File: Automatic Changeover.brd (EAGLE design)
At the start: 160 x 148.3 mm, 49 parts, among them IC1 ACS750LCA-050, IC2 XMEGA16A4A, IC4 ACS750LCA-050, IC5 ACS750LCA-050, K1 S216SE1, K2 S216SE1, K3 S216SE1, K4 S216SE1, K5 S216SE1, K6 S216SE1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

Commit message: good arrangement
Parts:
- moved IC1 74.3 mm to (142.2, 66.0), turned to 180 degrees
- moved T4 57.5 mm to (88.9, 111.8), turned to 90 degrees
- moved K1 49.5 mm to (132.1, 125.7), turned to 0 degrees
- moved B1 48.4 mm to (135.9, 10.2), turned to 180 degrees
- moved K3 46.0 mm to (87.6, 125.7), turned to 0 degrees
- moved T3 40.3 mm to (111.8, 111.8), turned to 90 degrees
- moved IC4 36.6 mm to (114.3, 66.0), turned to 180 degrees
- moved K2 36.1 mm to (110.5, 125.7), turned to 0 degrees
- moved T1 35.2 mm to (132.1, 110.5), turned to 90 degrees
- moved K4 34.3 mm to (88.9, 99.1), turned to 180 degrees
- moved C4 33.2 mm to (135.9, 50.8), turned to 180 degrees
- moved K6 29.2 mm to (133.3, 99.1), turned to 180 degrees
- moved B3 18.2 mm to (135.9, 25.4), turned to 180 degrees
- moved IC5 16.5 mm to (86.4, 66.0), turned to 180 degrees
- moved B4 13.3 mm to (135.9, 40.6), turned to 180 degrees
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
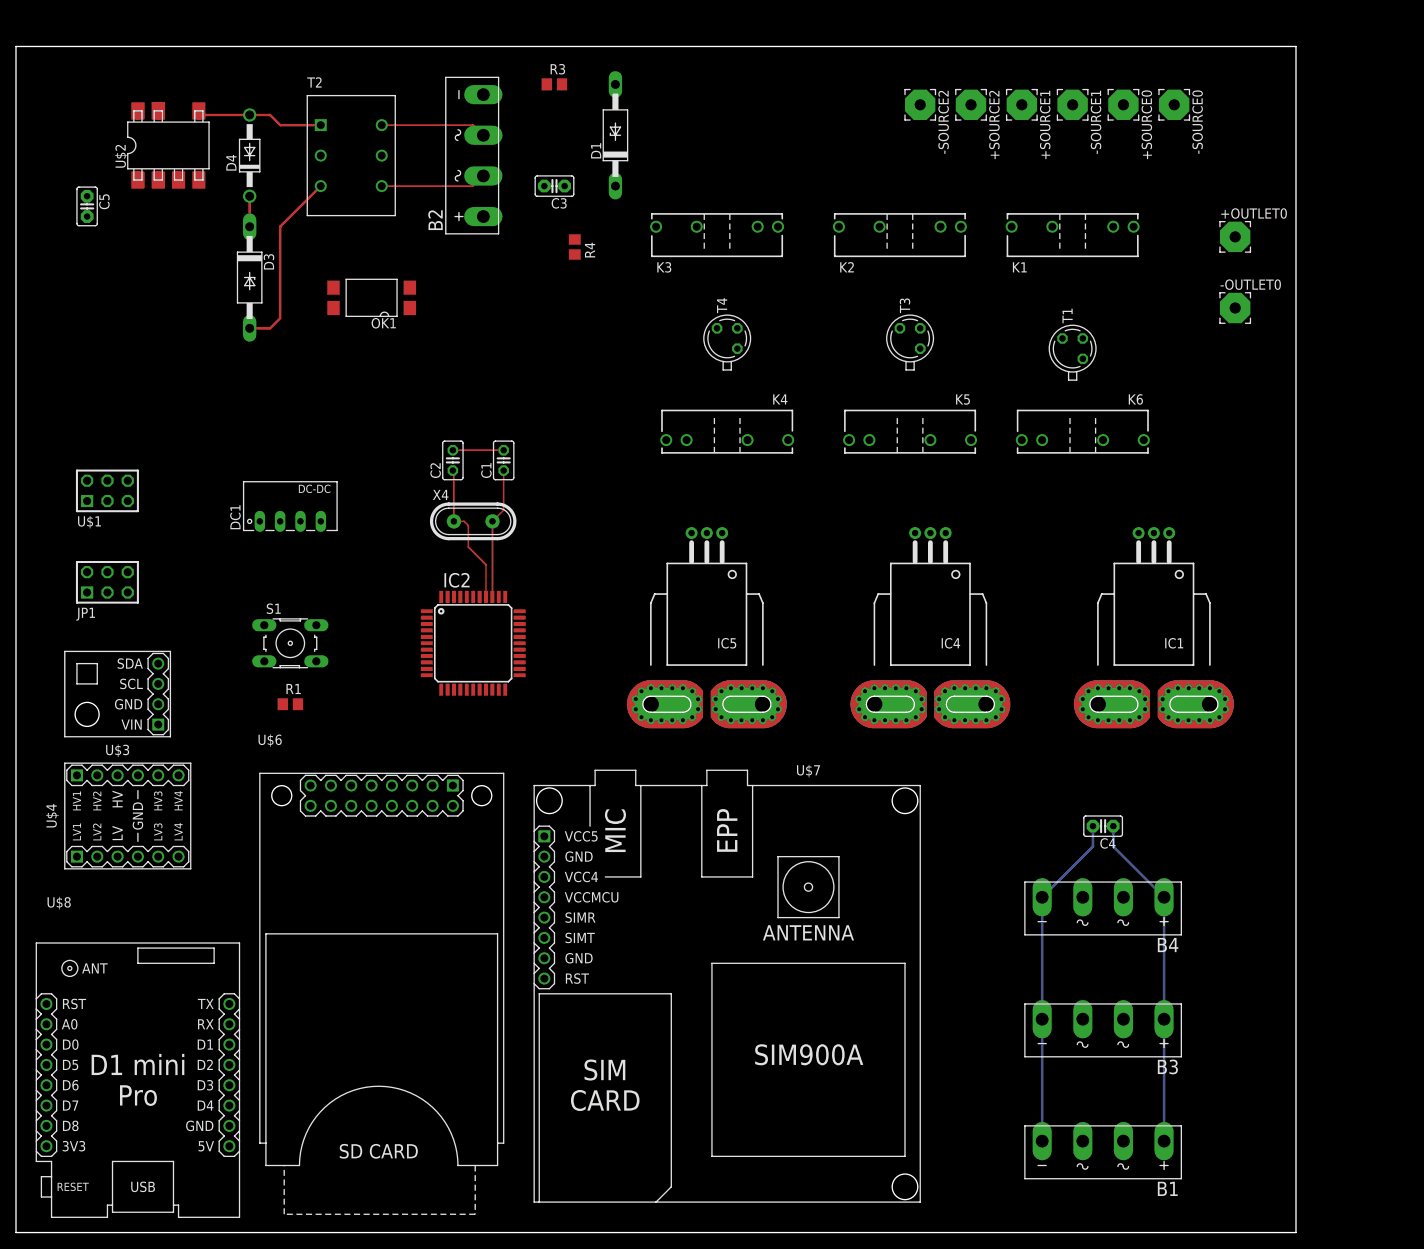
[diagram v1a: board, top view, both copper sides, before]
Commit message: added 100mil trace to connect AC wires
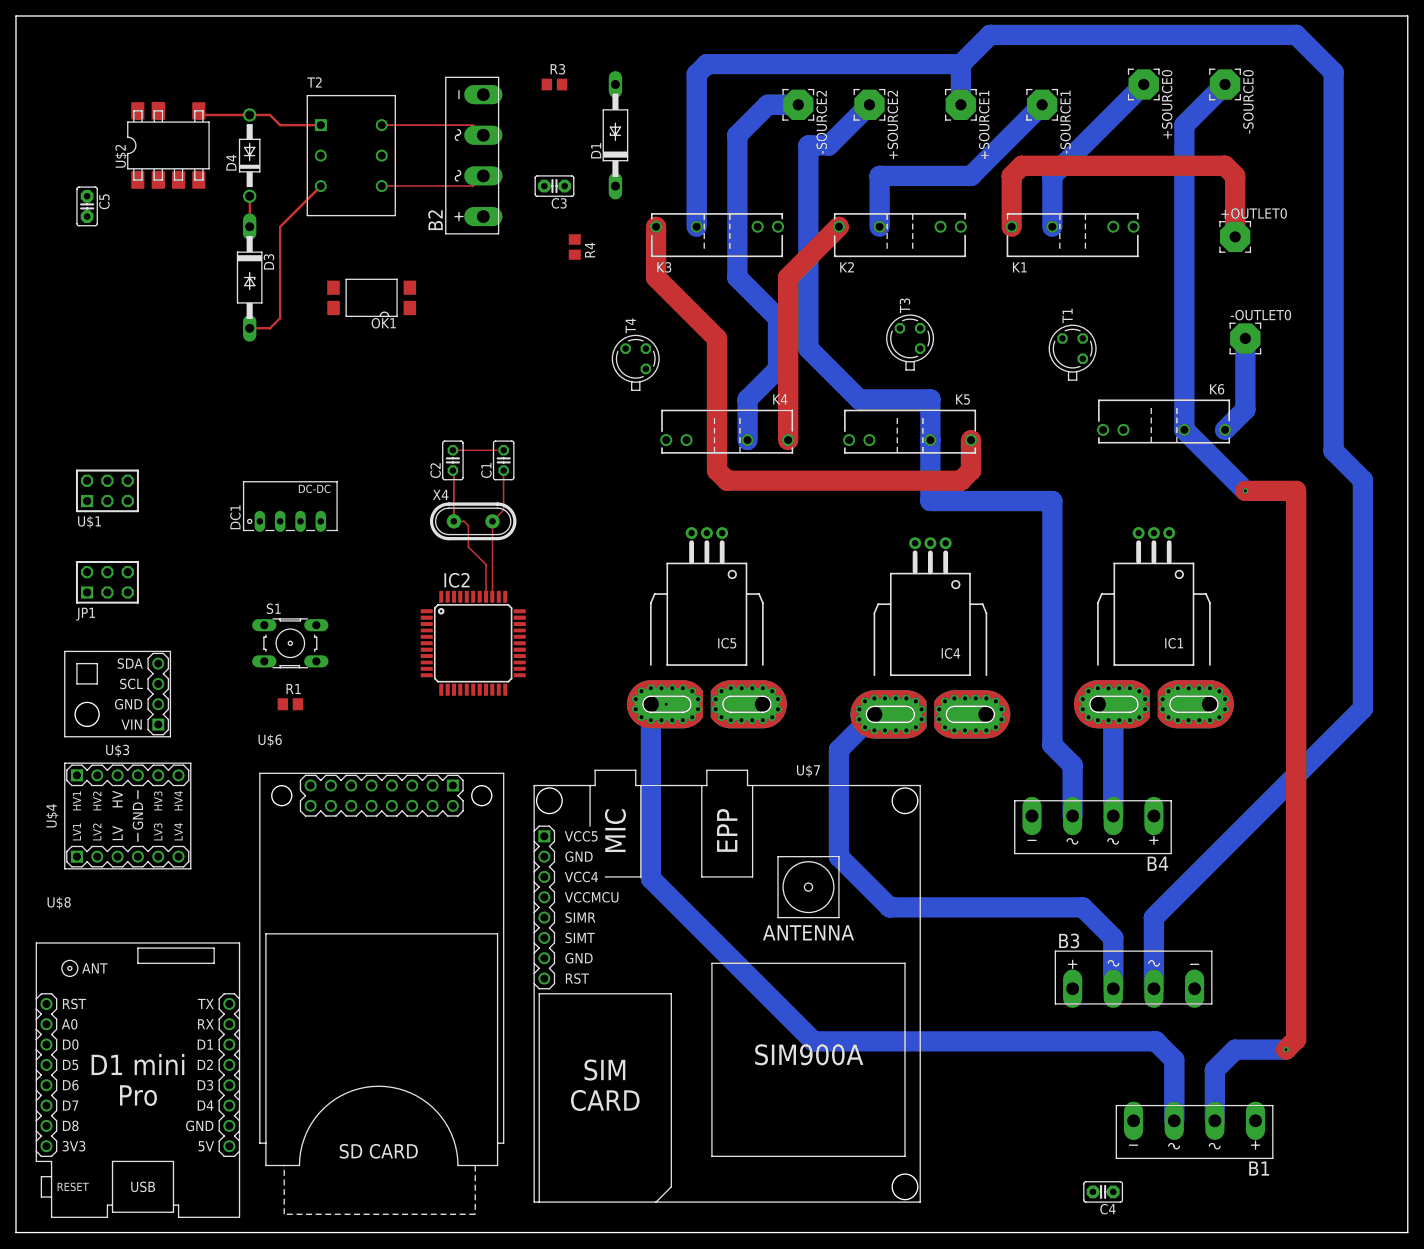
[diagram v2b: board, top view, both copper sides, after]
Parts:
- moved C4 45.7 mm to (135.9, 5.08)
- moved -SOURCE2 15.2 mm to (97.8, 141.0)
- moved +SOURCE2 12.7 mm to (106.7, 141.0)
- moved B1 11.7 mm to (147.3, 12.7)
- moved T4 11.7 mm to (77.5, 109.2)
- moved K6 10.2 mm to (143.5, 100.3)
- moved B4 10.2 mm to (134.6, 50.8)
- moved +SOURCE1 7.62 mm to (118.1, 141.0)
- moved B3 7.41 mm to (139.7, 31.8), turned to 0 degrees
- moved -SOURCE0 6.84 mm to (151.1, 143.5)
- moved -OUTLET0 4.02 mm to (153.7, 111.8)
- moved -SOURCE1 3.81 mm to (128.3, 141.0)
- moved +SOURCE0 3.59 mm to (141.0, 143.5)
- moved IC4 1.27 mm to (114.3, 64.8)
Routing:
- net +SOURCE1: track 0.00 -> 234.6 mm
- net -SOURCE0: track 0.00 -> 149.1 mm, vias 0 -> 2
- net +SOURCE2: track 0.00 -> 121.4 mm
- net N$16: track 0.00 -> 104.2 mm, vias 0 -> 1
- net +OUTLET0: track 0.00 -> 70.2 mm
- net N$20: track 0.00 -> 64.5 mm
- net -SOURCE2: track 0.00 -> 51.0 mm
- net N$47: track 0.00 -> 43.0 mm
- net N$41: track 42.0 -> 0.00 mm
- net N$17: track 65.0 -> 23.0 mm
- net -SOURCE1: track 0.00 -> 31.3 mm
- net -OUTLET0: track 0.00 -> 29.3 mm
- net +SOURCE0: track 0.00 -> 22.5 mm
- net N$14: track 0.00 -> 14.0 mm
- net N$32: track 0.00 -> 12.5 mm
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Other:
- board size 160 x 148.3 mm -> 174 x 152.1 mm

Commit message: Finished manually routing AC wires
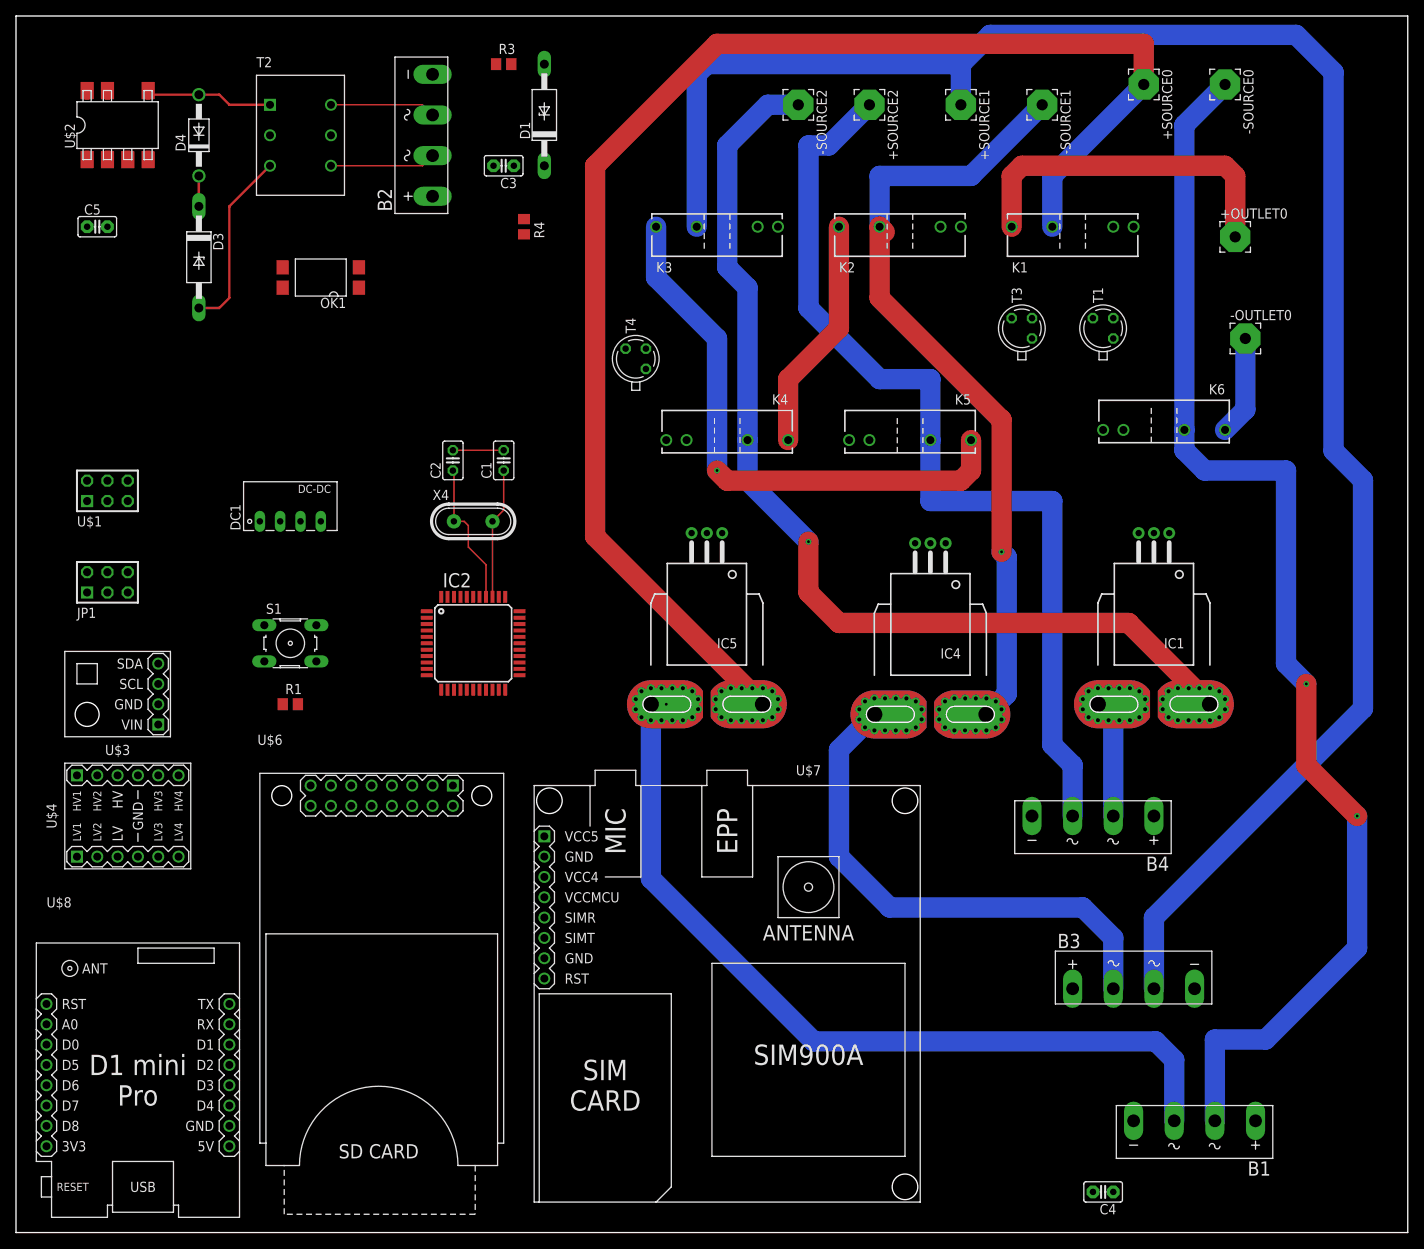
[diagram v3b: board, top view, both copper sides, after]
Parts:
- moved T3 14.0 mm to (125.7, 113.0)
- moved D1 9.25 mm to (66.0, 139.7)
- moved R3 6.84 mm to (61.0, 146.1)
- moved U$2 6.84 mm to (12.7, 138.4)
- moved D3 6.84 mm to (22.9, 121.9)
- moved B2 6.84 mm to (50.8, 137.2)
- moved C3 6.84 mm to (61.0, 133.3)
- moved D4 6.84 mm to (22.9, 137.2)
- moved OK1 6.84 mm to (38.1, 119.4)
- moved R4 6.84 mm to (63.5, 125.7)
- moved T2 6.84 mm to (35.6, 137.2)
- moved T1 4.58 mm to (135.9, 113.0)
- moved C5 2.84 mm to (10.2, 125.7), turned to 0 degrees
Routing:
- net +SOURCE0: track 22.5 -> 178.5 mm
- net -SOURCE2: track 51.0 -> 127.0 mm, vias 0 -> 1
- net -SOURCE1: track 31.3 -> 99.9 mm, vias 0 -> 1
- net -SOURCE0: track 149.1 -> 157.6 mm
- net +SOURCE2: track 121.4 -> 119.9 mm
- net +OUTLET0: vias 0 -> 1

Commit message: correcting route errors
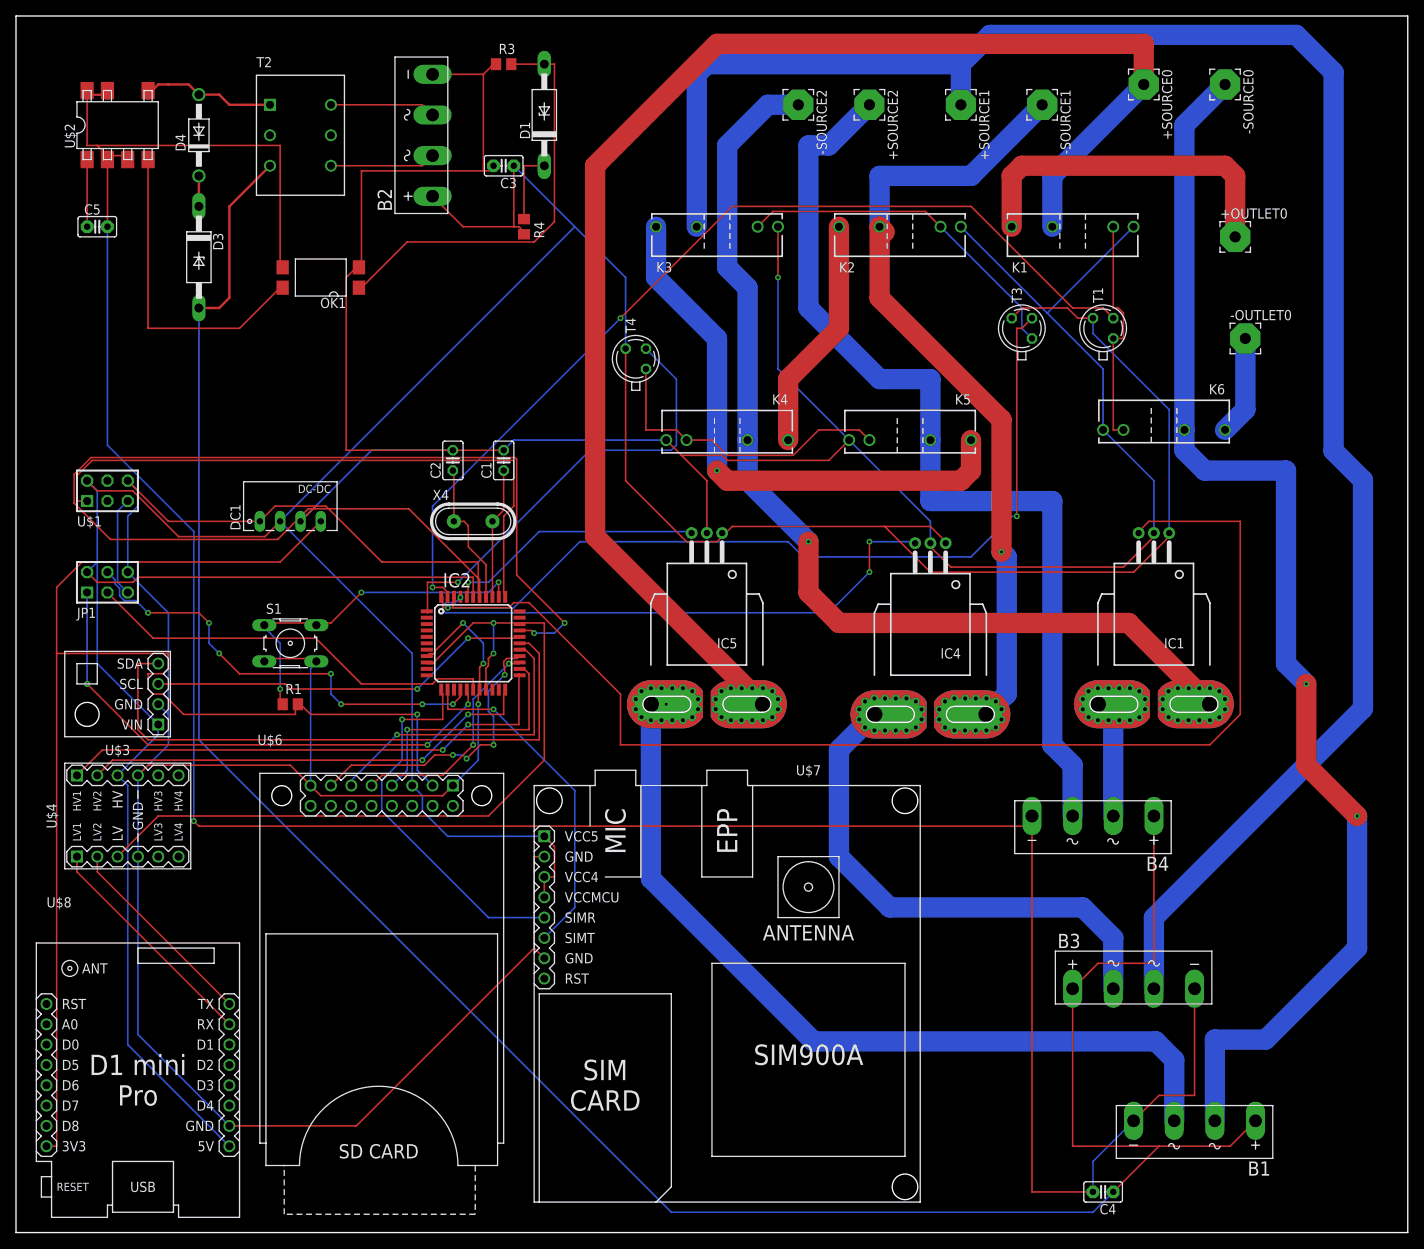
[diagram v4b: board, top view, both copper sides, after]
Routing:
- net GND: track 6.35 -> 768.7 mm, vias 1 -> 6
- net +5V: track 0.00 -> 491.2 mm
- net N$41: track 0.00 -> 336.0 mm, vias 0 -> 1
- net N$17: track 23.0 -> 298.6 mm
- net 3V3: track 0.00 -> 174.6 mm, vias 0 -> 1
- net IN2: track 0.00 -> 150.3 mm
- net OUT0: track 0.00 -> 119.3 mm, vias 0 -> 2
- net OUT1: track 0.00 -> 105.5 mm, vias 0 -> 2
- net VCC: track 0.00 -> 101.2 mm, vias 0 -> 2
- net PDI_DATA: track 0.00 -> 77.5 mm
- net TEMP_SDA: track 0.00 -> 75.3 mm
- net IN1: track 0.00 -> 68.4 mm, vias 0 -> 3
- net MISO: track 0.00 -> 66.2 mm, vias 0 -> 3
- net WIFI_RX: track 0.00 -> 64.4 mm, vias 0 -> 2
- net WIFI_TX: track 0.00 -> 57.1 mm, vias 0 -> 2
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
